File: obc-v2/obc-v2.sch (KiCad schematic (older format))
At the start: 37 parts

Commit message: obc-v2: Fix reset circuit to prevent accidental triggering. Add i2c/uart connectors, SWD debugger header, and LED resistors.
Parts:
- added J? (x2): Conn_01x04, symbol Connector_Generic:Conn_01x04
- added R?: 130, symbol Device:R_US
- added R? (x2): 10, symbol Device:R_US
- J?: symbol Connector_Generic:Conn_01x01 -> Connector_Generic:Conn_01x02
- J?: value Conn_02x05_Counter_Clockwise -> Conn_02x05_Odd_Even; symbol Connector_Generic:Conn_02x05_Counter_Clockwise -> Connector_Generic:Conn_02x05_Odd_Even
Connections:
- net *RESET: now also J?.10 (Pin_10); no longer J?.6 (Pin_6)
- net +3V3: now also J?.5 (Pin_5), J?.1 (Pin_1), J?.4 (Pin_4)
- net GND: now also J?.2 (Pin_2), J?.4 (Pin_4), J?.5 (Pin_5), J?.9 (Pin_9), J?.1 (Pin_1), J?.4 (Pin_4); no longer J?.2 (Pin_2)
- net GPIO0: now also U?.25 (PA27), R?.2; no longer D?.1 (RK), U?.5 (PA04)
- net GPIO1: now also R?.2; no longer D?.2 (GK)
- net GPIO2: now also R?.2; no longer D?.3 (BK)
- net GPIO8: no longer J?.4 (Pin_4)
- net RX: now also J?.3 (Pin_3)
- net SCL: now also J?.3 (Pin_3)
- net SDA: now also J?.2 (Pin_2)
- net SWDCLK: now also J?.4 (Pin_4); no longer J?.9 (Pin_9)
- net SWDIO: now also J?.2 (Pin_2); no longer J?.10 (Pin_10)
- net TX: now also J?.2 (Pin_2)
- net VMEAS: now also U?.5 (PA04); no longer U?.25 (PA27)
- new net: D?.1 (RK), R?.1
- new net: D?.2 (GK), R?.1
- new net: D?.3 (BK), R?.1
- no-connect marks 10 -> 8
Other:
- note added: "UART and I2C Connectors"
- note added: "Voltage Divider\nfor Battery Charge\nMeasurement"
- note removed: "Voltage Divider\nfor Battery Voltage Measurement"
- moved on the sheet: C?, D?, J?, R?, U?, X?

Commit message: obc-v2: Add I2C pull-up resistors
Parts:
- added R? (x2): 10k, symbol Device:R_US
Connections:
- net +3V3: now also R?.1, R?.1
- net SCL: now also R?.2
- net SDA: now also R?.2
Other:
- note added: "I2C Pull-Up\nResistors"
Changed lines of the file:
@@
 Wire Notes Line
 	7100 5200 7100 6150
+$Comp
+L Device:R_US R?
+U 1 1 614E4A8D
+P 6650 5700
+F 0 "R?" H 6700 5850 50  0000 L CNN
+F 1 "10k" V 6750 5600 50  0000 L CNN
+F 2 "" V 6690 5690 50  0001 C CNN
+F 3 "~" H 6650 5700 50  0001 C CNN
+	1    6650 5700
+	1    0    0    -1
+$EndComp
+$Comp
+L Device:R_US R?
+U 1 1 614E4DBC
+P 6350 5700
+F 0 "R?" H 6200 5850 50  0000 L CNN
+F 1 "10k" V 6250 5600 50  0000 L CNN
+F 2 "" V 6390 5690 50  0001 C CNN
+F 3 "~" H 6350 5700 50  0001 C CNN
+	1    6350 5700
+	1    0    0    -1
+$EndComp
+Text GLabel 6350 5850 3    50   Input ~ 0
+SDA
+Text GLabel 6650 5850 3    50   Input ~ 0
+SCL
+$Comp
+L power:+3V3 #PWR?
+U 1 1 614E84A3
+P 6350 5450
+F 0 "#PWR?" H 6350 5300 50  0001 C CNN
+F 1 "+3V3" H 6365 5623 50  0000 C CNN
+F 2 "" H 6350 5450 50  0001 C CNN
+F 3 "" H 6350 5450 50  0001 C CNN
+	1    6350 5450
+	1    0    0    -1
+$EndComp
+Wire Wire Line
+	6350 5550 6350 5450
+Wire Wire Line
+	6650 5550 6650 5450
+Wire Wire Line
+	6650 5450 6350 5450
+Connection ~ 6350 5450
+Text Notes 6250 6250 0    50   ~ 0
+I2C Pull-Up\nResistors
+Wire Notes Line
+	6850 5200 6850 6300
+Wire Notes Line
+	6850 6300 6150 6300
+Wire Notes Line
+	6150 6300 6150 5200
+Wire Notes Line
+	6150 5200 6850 5200
 $EndSCHEMATC

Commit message: obc-v2: Minor changes
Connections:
- net +3V3: now also J?.4 (Pin_4); no longer J?.1 (Pin_1)
- net GND: now also J?.1 (Pin_1), J?.1 (Pin_1), J?.1 (Pin_1), J?.1 (Pin_1); no longer J?.2 (Pin_2), J?.2 (Pin_2), J?.4 (Pin_4), J?.4 (Pin_4)
- net GPIO5: now also J?.2 (Pin_2); no longer J?.1 (Pin_1)
- net GPIO6: now also J?.3 (Pin_3); no longer J?.2 (Pin_2)
- net GPIO7: now also J?.4 (Pin_4); no longer J?.3 (Pin_3)
- net RX: now also J?.2 (Pin_2); no longer J?.3 (Pin_3)
- net THERMAL: now also J?.2 (Pin_2); no longer J?.1 (Pin_1)
- net TX: now also J?.3 (Pin_3); no longer J?.2 (Pin_2)
- net VIN: now also J?.2 (Pin_2); no longer J?.1 (Pin_1)
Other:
- moved on the sheet: C?, D?, FB?, J?, R?, SW?

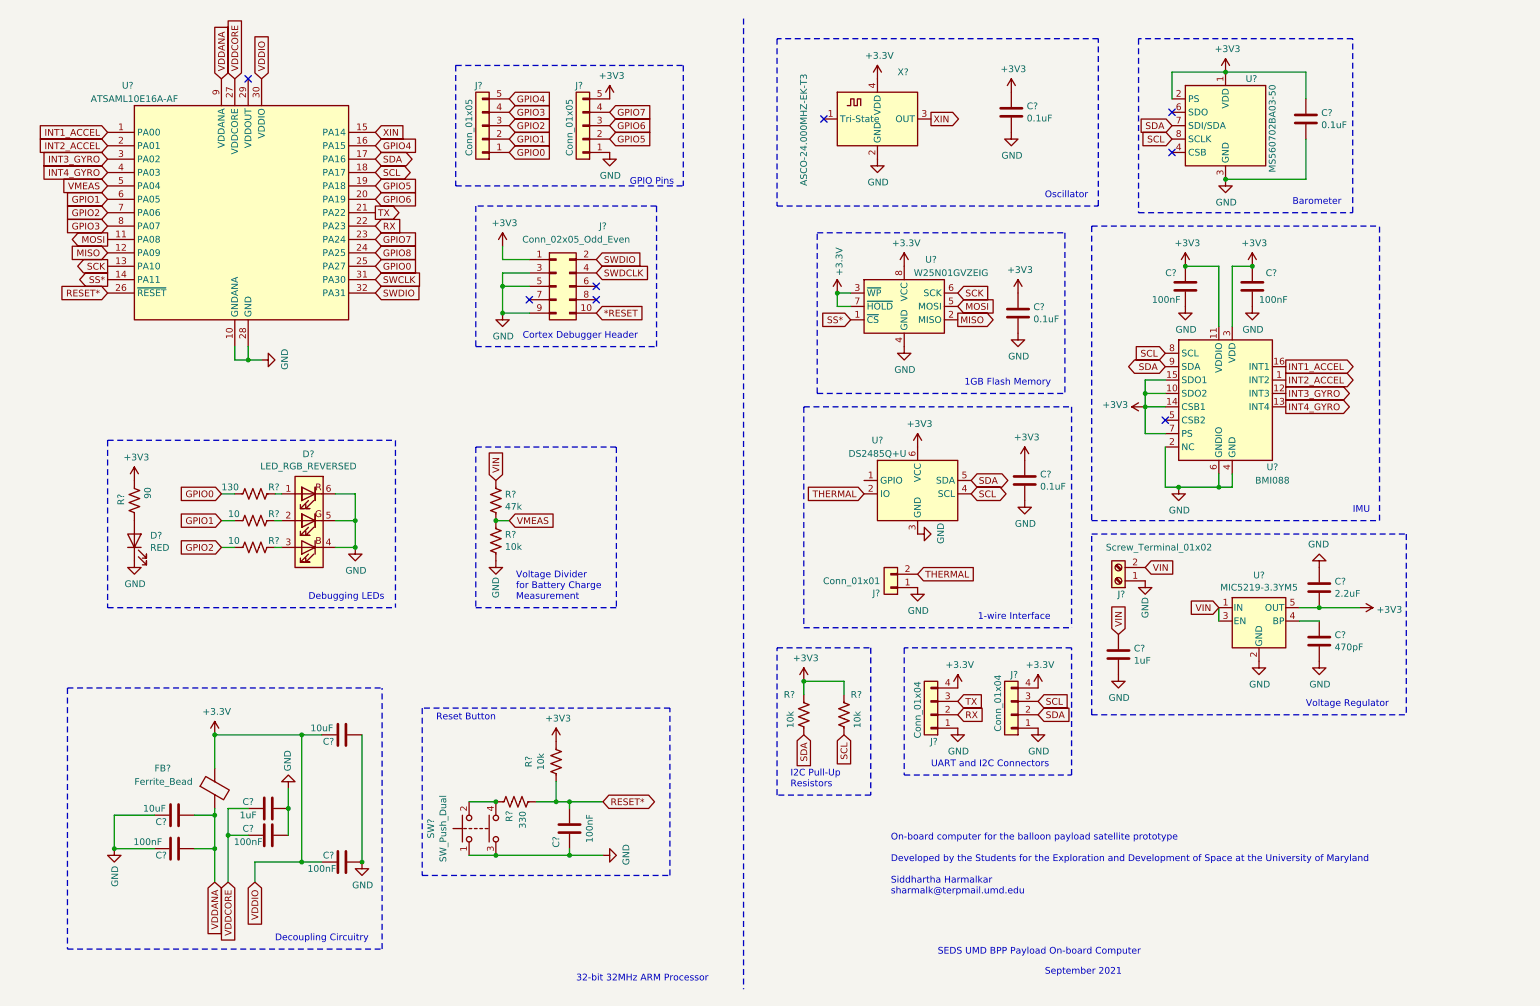
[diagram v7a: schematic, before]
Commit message: obc-v2: Add test pads
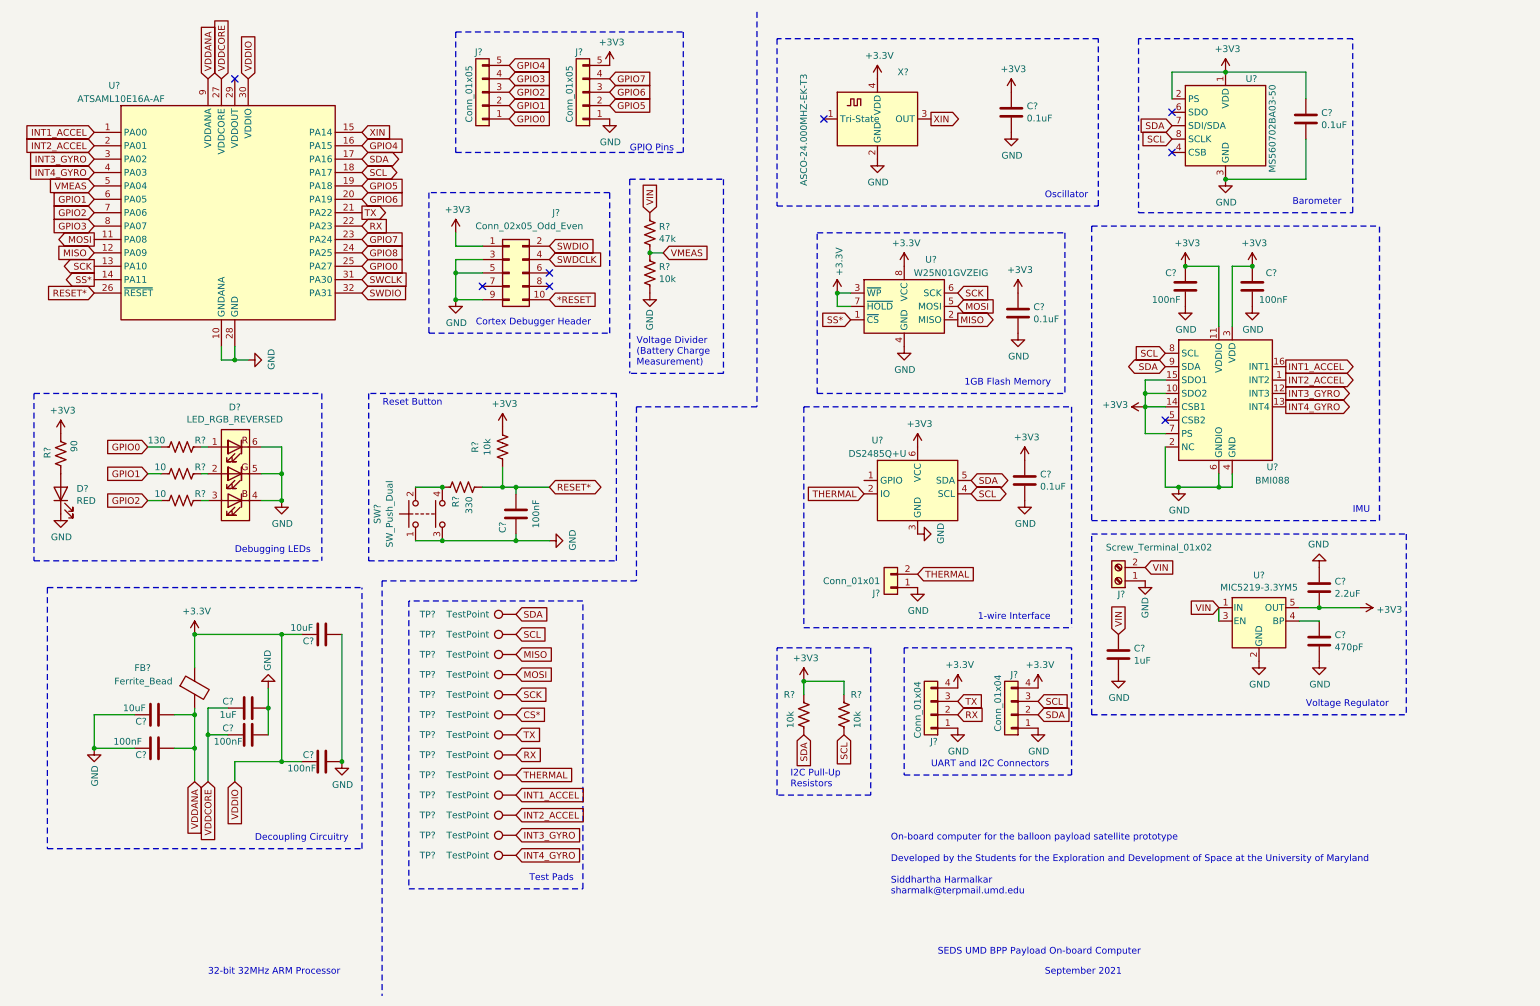
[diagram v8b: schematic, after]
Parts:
- added TP? (x13): TestPoint, symbol Connector:TestPoint
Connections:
- net INT1_ACCEL: now also TP?.1
- net INT2_ACCEL: now also TP?.1
- net INT3_GYRO: now also TP?.1
- net INT4_GYRO: now also TP?.1
- net MISO: now also TP?.1
- net MOSI: now also TP?.1
- net RX: now also TP?.1
- net SCK: now also TP?.1
- net SCL: now also TP?.1
- net SDA: now also TP?.1
- net THERMAL: now also TP?.1
- net TX: now also TP?.1
- new net CS*: TP?.1
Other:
- note added: "Test Pads"
- note added: "Voltage Divider\n(Battery Charge\nMeasurement)"
- note removed: "Voltage Divider\nfor Battery Charge\nMeasurement"
- moved on the sheet: C?, D?, FB?, J?, R?, SW?, U?
